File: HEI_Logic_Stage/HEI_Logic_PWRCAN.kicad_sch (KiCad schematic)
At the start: 28 parts, among them J7 RJ_{1}, J8 RJ_{2}, SW3 SW_SPST, U11 B1203XT-1WR3, U12 5V_Converter_R-78E5.0-0.5, U13 5V_Converter_R-78E5.0-0.5, U14 ADM3058EBRIZ, U2 TMH 1212S

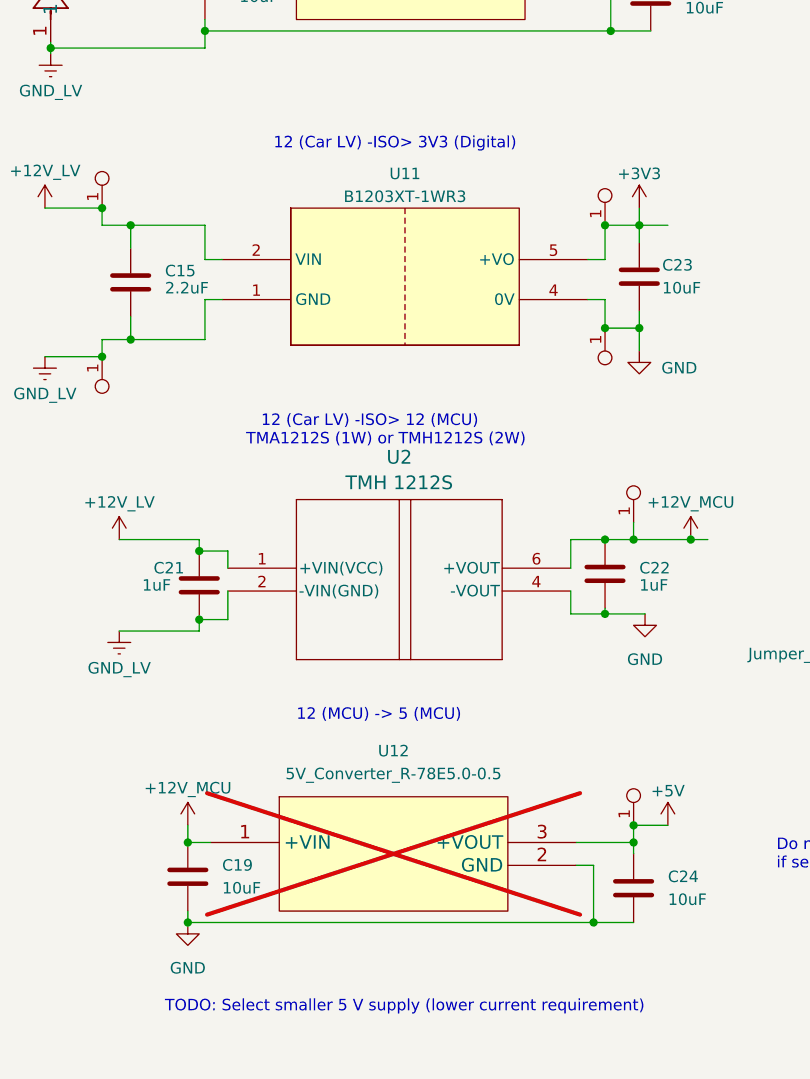
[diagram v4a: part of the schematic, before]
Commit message: almost completed new logic layout
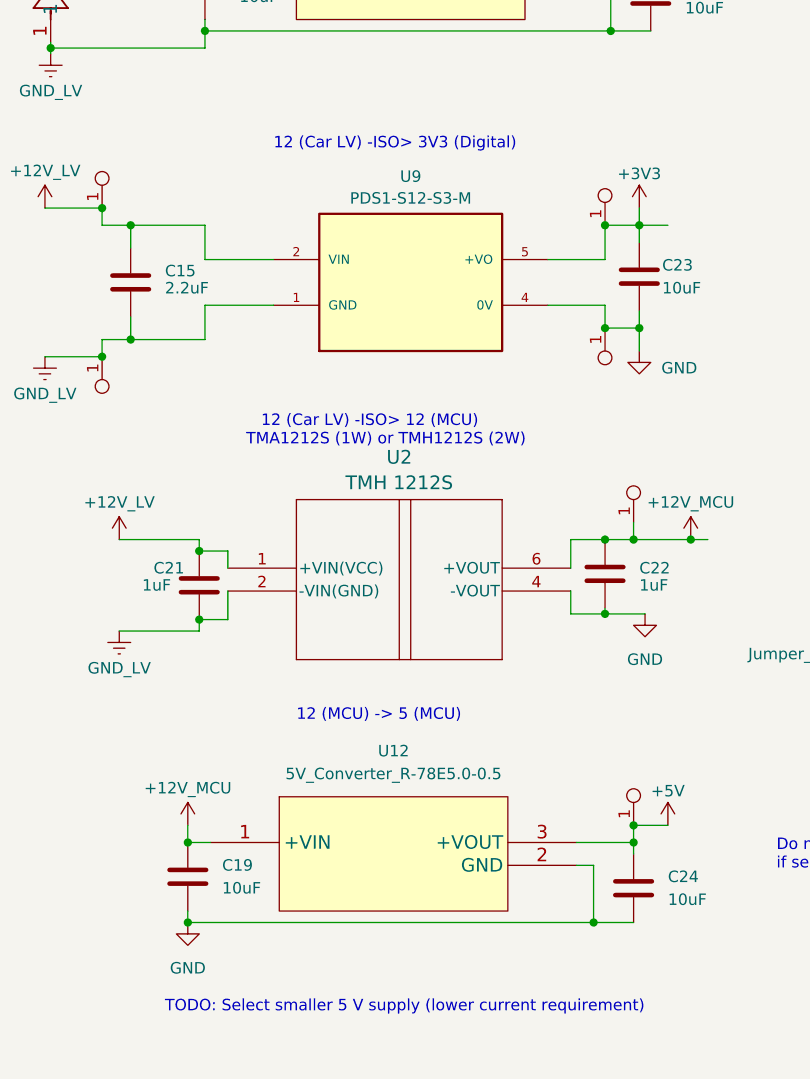
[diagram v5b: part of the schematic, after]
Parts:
- removed U11: B1203XT-1WR3, GTSR_KiCAD_Footprints:B_XT-1WR3_MNS-M, symbol GTSR_symbol_lib:B1203XT-1WR3
- added U9: PDS1-S12-S3-M, HEI_Logic:CONV_PDS1-S12-S3-M, symbol HEI_Logic:PDS1-S12-S3-M
- U12: now fitted
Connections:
- net +12V_LV: now also U9.2 (VIN)
- net +3V3: now also U9.5 (+VO)
- net GND: now also U9.4 (0V)
- net GND_LV: now also U9.1 (GND)
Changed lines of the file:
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@@
 	)
 	(junction
-		(at 60.96 52.07)
+		(at 105.41 93.98)
 		(diameter 0)
 		(color 0 0 0 0)
 	)
 	(junction
-		(at 49.53 97.155)
+		(at 60.96 52.07)
 		(diameter 0)
 		(color 0 0 0 0)
 	)
 	(junction
-		(at 52.705 95.25)
+		(at 49.53 97.155)
 		(diameter 0)
 		(color 0 0 0 0)
 	)
 	(junction
-		(at 110.49 52.07)
+		(at 52.705 95.25)
 		(diameter 0)
 		(color 0 0 0 0)
 	)
 	(junction
-		(at 105.41 93.98)
+		(at 110.49 52.07)
 		(diameter 0)
 		(color 0 0 0 0)
@@
 	(wire
 		(pts
-			(xy 105.41 90.805) (xy 105.41 93.98)
-		)
-		(stroke
-			(width 0)
-			(type default)
-		)
-	)
-	(wire
-		(pts
 			(xy 43.815 62.865) (xy 43.815 62.23)
 		)
@@
 	(wire
 		(pts
+			(xy 60.96 91.44) (xy 60.96 95.25)
+		)
+		(stroke
+			(width 0)
+			(type default)
+		)
+	)
+	(wire
+		(pts
 			(xy 60.96 62.865) (xy 60.96 60.96)
 		)
@@
 	(wire
 		(pts
-			(xy 60.96 90.805) (xy 62.865 90.805)
+			(xy 104.14 160.02) (xy 104.14 153.67)
 		)
 		(stroke
@@
 	(wire
 		(pts
-			(xy 104.14 160.02) (xy 104.14 153.67)
+			(xy 59.055 149.225) (xy 59.055 151.13)
 		)
 		(stroke
@@
 	(wire
 		(pts
-			(xy 59.055 149.225) (xy 59.055 151.13)
+			(xy 110.49 52.07) (xy 110.49 53.34)
 		)
 		(stroke
@@
 	(wire
 		(pts
-			(xy 110.49 52.07) (xy 110.49 53.34)
+			(xy 101.6 125.73) (xy 105.41 125.73)
 		)
 		(stroke
@@
 	(wire
 		(pts
-			(xy 101.6 125.73) (xy 105.41 125.73)
+			(xy 105.41 91.44) (xy 105.41 93.98)
 		)
 		(stroke
@@
 	(wire
 		(pts
-			(xy 60.96 90.805) (xy 60.96 95.25)
-		)
-		(stroke
-			(width 0)
-			(type default)
-		)
-	)
-	(wire
-		(pts
 			(xy 60.96 82.55) (xy 60.96 86.36)
 		)
@@
 	(wire
 		(pts
+			(xy 99.06 91.44) (xy 105.41 91.44)
+		)
+		(stroke
+			(width 0)
+			(type default)
+		)
+	)
+	(wire
+		(pts
 			(xy 241.3 86.36) (xy 241.3 88.265)
 		)
@@
 	(wire
 		(pts
-			(xy 103.505 86.36) (xy 105.41 86.36)
+			(xy 99.06 86.36) (xy 105.41 86.36)
 		)
 		(stroke
@@
 	(wire
 		(pts
+			(xy 68.58 91.44) (xy 60.96 91.44)
+		)
+		(stroke
+			(width 0)
+			(type default)
+		)
+	)
+	(wire
+		(pts
 			(xy 109.22 96.52) (xy 109.22 93.98)
 		)
@@
 	(wire
 		(pts
-			(xy 103.505 90.805) (xy 105.41 90.805)
-		)
-		(stroke
-			(width 0)
-			(type default)
-		)
-	)
-	(wire
-		(pts
 			(xy 229.235 59.69) (xy 226.06 59.69)
 		)
@@
 	(wire
 		(pts
-			(xy 60.96 86.36) (xy 62.865 86.36)
+			(xy 60.96 86.36) (xy 68.58 86.36)
 		)
 		(stroke
@@
 	)
 	(symbol
-		(lib_id "GTSR_symbol_lib:B1203XT-1WR3")
-		(at 83.185 78.74 0)
-		(unit 1)
-		(exclude_from_sim no)
-		(in_bom yes)
-		(on_board yes)
-		(dnp no)
-		(fields_autoplaced yes)
-		(property "Reference" "U11"
-			(at 83.185 76.835 0)
-			(effects
-				(font
-					(size 1.27 1.27)
-				)
-			)
-		)
-		(property "Value" "B1203XT-1WR3"
-			(at 83.185 79.375 0)
-			(effects
-				(font
-					(size 1.27 1.27)
-				)
-			)
-		)
-		(property "Footprint" "GTSR_KiCAD_Footprints:B_XT-1WR3_MNS-M"
-			(at 83.185 78.74 0)
-			(effects
-				(font
-					(size 1.27 1.27)
-				)
-				(hide yes)
-			)
-		)
-		(property "Datasheet" "https://www.digikey.com/en/products/detail/mornsun-america-llc/B1203XT-1WR3/16348385"
-			(at 83.185 78.74 0)
-			(effects
-				(font
-					(size 1.27 1.27)
-				)
-				(hide yes)
-			)
-		)
-		(property "Description" ""
-			(at 83.185 78.74 0)
-			(effects
-				(font
-					(size 1.27 1.27)
-				)
-				(hide yes)
-			)
-		)
-		(property "Populate" ""
-			(at 83.185 78.74 0)
-			(effects
-				(font
-					(size 1.27 1.27)
-				)
-			)
-		)
-		(pin "1"
-		)
-		(pin "2"
-		)
-		(pin "4"
-		)
-		(pin "5"
-		)
-		(pin "8"
-		)
-		(instances
-			(project "HEI_Logic"
-				(path "/9d05e1b7-f292-46e2-9203-5654fb6f820e/0de18315-f7ce-42ca-adfe-a88a58247ef3"
-					(reference "U11")
-					(unit 1)
-				)
-			)
-		)
-	)
-	(symbol
 		(lib_id "power:GNDREF")
 		(at 243.205 99.06 0)
@@
 		(in_bom yes)
 		(on_board yes)
-		(dnp yes)
+		(dnp no)
 		(fields_autoplaced yes)
 		(property "Reference" "U12"
@@
 					(unit 1)
 				)
+			)
+		)
+	)
+	(symbol
+		(lib_id "HEI_Logic:PDS1-S12-S3-M")
+		(at 83.82 88.9 0)
+		(unit 1)
+		(exclude_from_sim no)
+		(in_bom yes)
+		(on_board yes)
+		(dnp no)
+		(fields_autoplaced yes)
+		(property "Reference" "U9"
+			(at 83.82 77.1355 0)
+			(effects
+				(font
+					(size 1.27 1.27)
+				)
+			)
+		)
+		(property "Value" "PDS1-S12-S3-M"
+			(at 83.82 79.5598 0)
+			(effects
+				(font
+					(size 1.27 1.27)
+				)
+			)
+		)
+		(property "Footprint" "HEI_Logic:CONV_PDS1-S12-S3-M"
+			(at 83.82 88.9 0)
+			(effects
+				(font
+					(size 1.27 1.27)
+				)
+				(justify bottom)
+				(hide yes)
+			)
+		)
+		(property "Datasheet" ""
+			(at 83.82 88.9 0)
+			(effects
+				(font
+					(size 1.27 1.27)
+				)
+				(hide yes)
+			)
+		)
+		(property "Description" ""
+			(at 83.82 88.9 0)
+			(effects
+				(font
+					(size 1.27 1.27)
+				)
+				(hide yes)
+			)
+		)
+		(property "MF" "CUI"
+			(at 83.82 88.9 0)
+			(effects
+				(font
+					(size 1.27 1.27)
+				)
+				(justify bottom)
+				(hide yes)
+			)
+		)
+		(property "DESCRIPTION" "PDS1 Series 1 W 12 VDC 84 mA Surface Mount DC-DC Isolated Converter"
+			(at 83.82 88.9 0)
+			(effects
+				(font
+					(size 1.27 1.27)
+				)
+				(justify bottom)
+				(hide yes)
+			)
+		)
+		(property "PACKAGE" "SMD-8 CUI"
+			(at 83.82 88.9 0)
+			(effects
+				(font
+					(size 1.27 1.27)
+				)
+				(justify bottom)
+				(hide yes)
+			)
+		)
+		(property "PRICE" "4.02 USD"
+			(at 83.82 88.9 0)
+			(effects
+				(font
+					(size 1.27 1.27)
+				)
+				(justify bottom)
+				(hide yes)
+			)
+		)
+		(property "MP" "PDS1-S12-S12-M"
+			(at 83.82 88.9 0)
+			(effects
+				(font
+					(size 1.27 1.27)
+				)
+				(justify bottom)
+				(hide yes)
+			)
+		)
+		(property "AVAILABILITY" "Bad"
+			(at 83.82 88.9 0)
+			(effects
+				(font
+					(size 1.27 1.27)
+				)
+				(justify bottom)
+				(hide yes)
+			)
+		)
+		(property "Populate" ""
+			(at 83.82 88.9 0)
+			(effects
+				(font
+					(size 1.27 1.27)
+				)
+			)
+		)
+		(pin "1"
+		)
+		(pin "4"
+		)
+		(pin "2"
+		)
+		(pin "5"
+		)
+		(instances
+			(project ""
+				(path "/9d05e1b7-f292-46e2-9203-5654fb6f820e/0de18315-f7ce-42ca-adfe-a88a58247ef3"
+					(reference "U9")
+					(unit 1)
+				)

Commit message: main portion of logic drc done
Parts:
- J8: now fitted
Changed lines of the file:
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@@
 		(in_bom yes)
 		(on_board yes)
-		(dnp yes)
+		(dnp no)
 		(property "Reference" "J8"
 			(at 239.395 71.755 0)

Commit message: schematic updates - logic
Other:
- note added: "12 (Car LV) -ISO> 12 (MCU) TMH1212S (2W)"
- note removed: "12 (Car LV) -ISO> 12 (MCU) TMA1212S (1W) or TMH1212S (2W)"
- note removed: "Do not populate 5V converter if selecting 12V"
- note removed: "TODO: Select smaller 5 V supply (lower current requirement)"
- moved on the sheet: C19, C24, U12

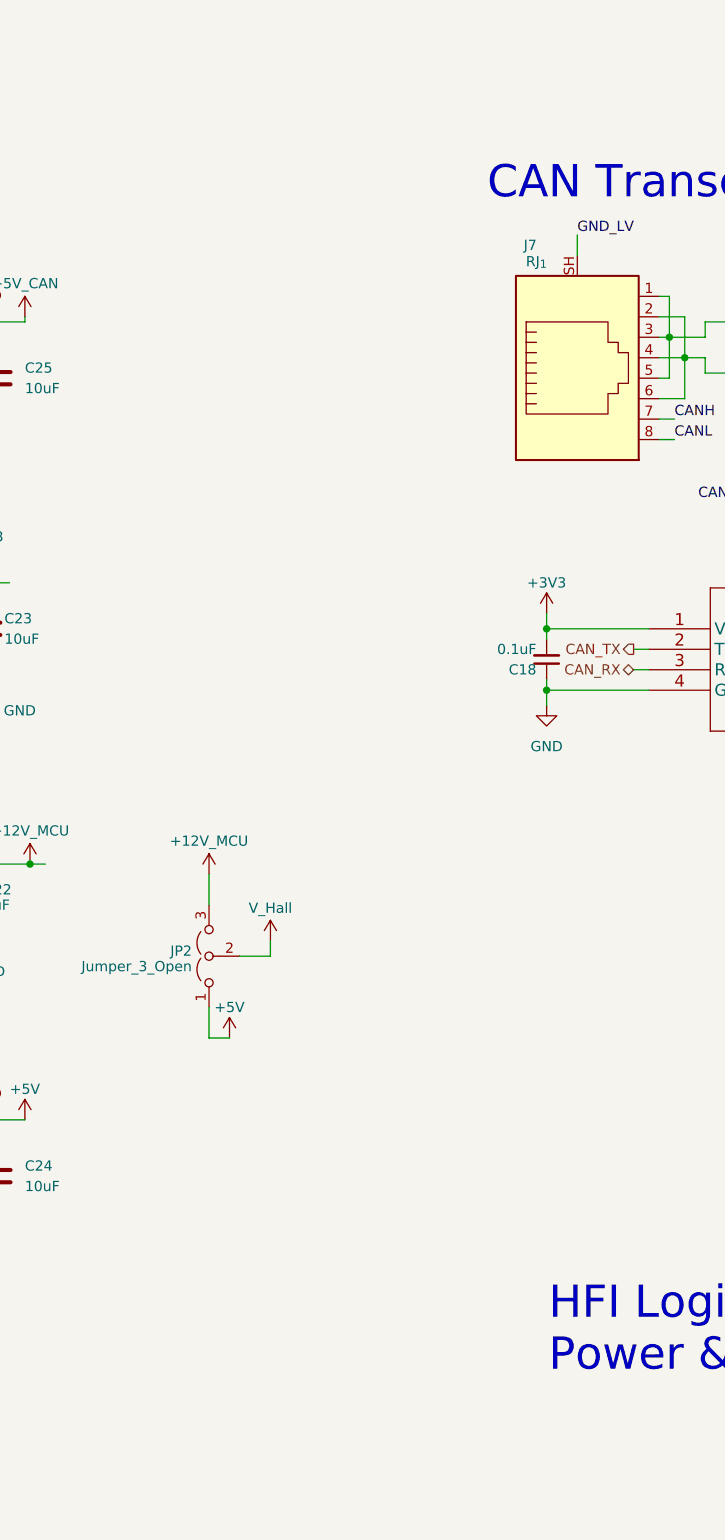
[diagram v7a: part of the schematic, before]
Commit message: added horizontal b2b connector info/3d model
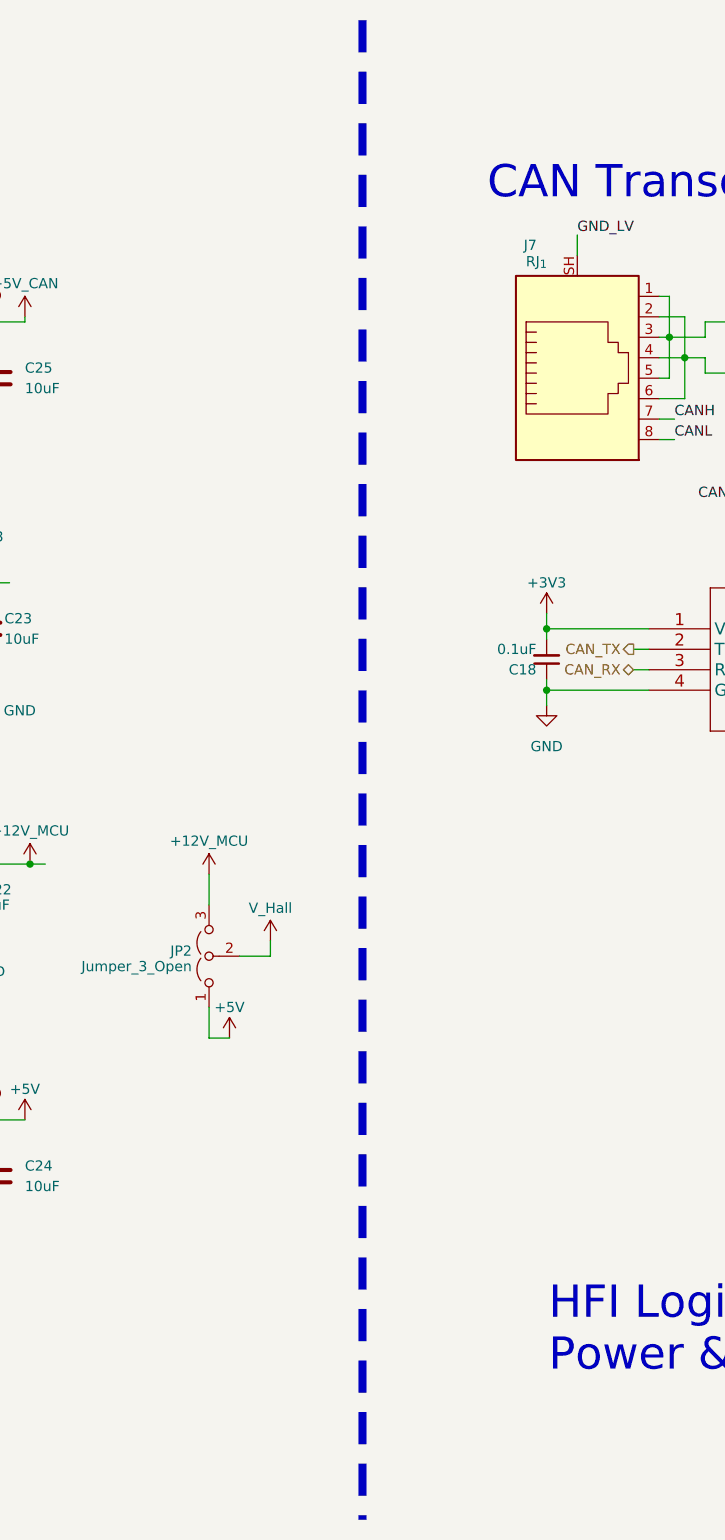
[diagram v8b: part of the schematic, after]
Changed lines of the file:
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@@
+		)
+	)
+	(polyline
+		(pts
+			(xy 156.21 12.7) (xy 156.21 198.882)
+		)
+		(stroke
+			(width 1)
+			(type dot)
 		)
 	)
